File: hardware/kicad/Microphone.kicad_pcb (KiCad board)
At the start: 2 copper layers, 60.1 x 40 mm, 24 parts, among them J1 POWER IN - 5V, J2 AUDIO OUT, U1 OPA1652D

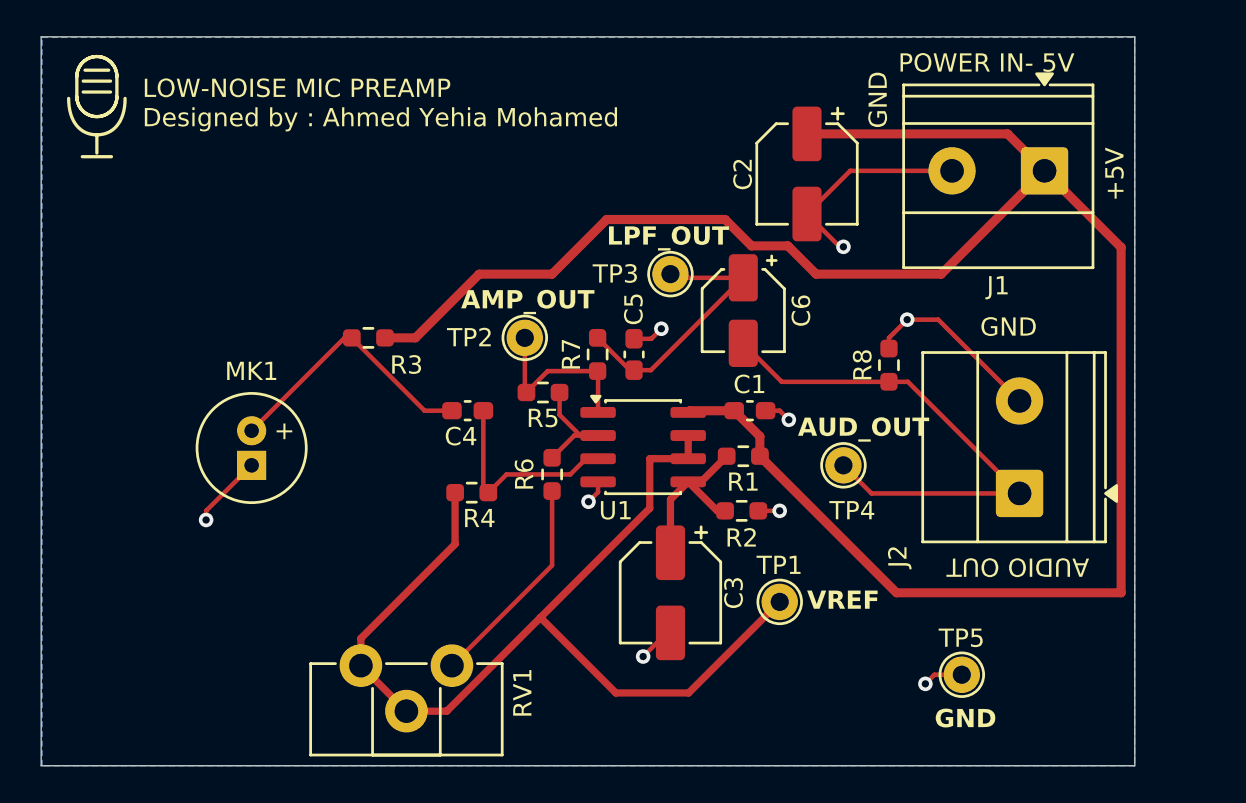
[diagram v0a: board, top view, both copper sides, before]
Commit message: Update microphone preamplifier PCB layout and schematic
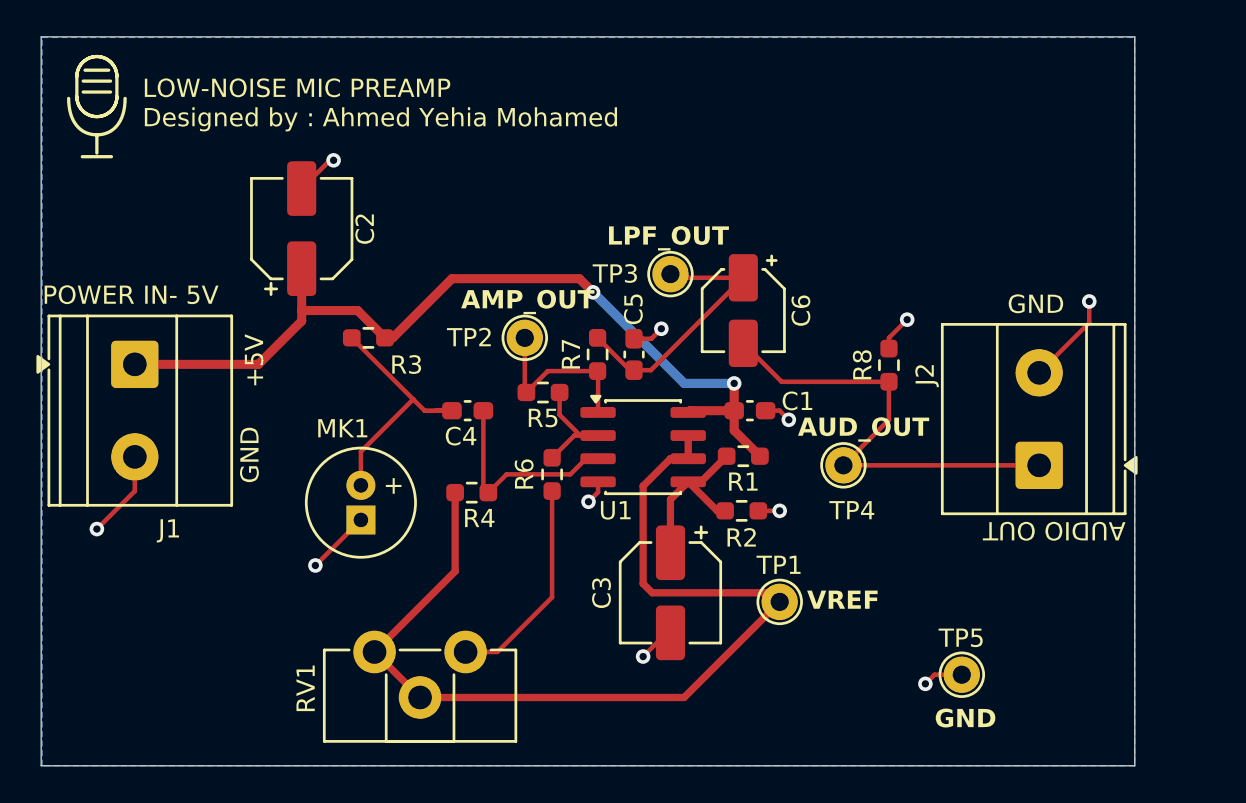
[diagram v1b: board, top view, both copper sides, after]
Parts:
- moved J1 51.1 mm to (105.1, 73.5), turned to -90 degrees
- moved C2 27.9 mm to (114.2, 66.0), turned to 90 degrees
- moved MK1 6.71 mm to (117.5, 81.0)
- moved J2 1.88 mm to (154.8, 79.0)
- moved RV1 1.06 mm to (123.2, 89.2)
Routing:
- net +5V: track 109.9 -> 48.3 mm, vias 0 -> 2
- net GND: track 35.7 -> 27.8 mm, vias 9 -> 11
- net /AUDIO_OUT: track 28.9 -> 25.2 mm
- net /VREF: track 56.2 -> 53.7 mm
- net /MIC_OUT: track 14.8 -> 14.0 mm

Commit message: Sync KiCad sources to manufactured AD8656 revision
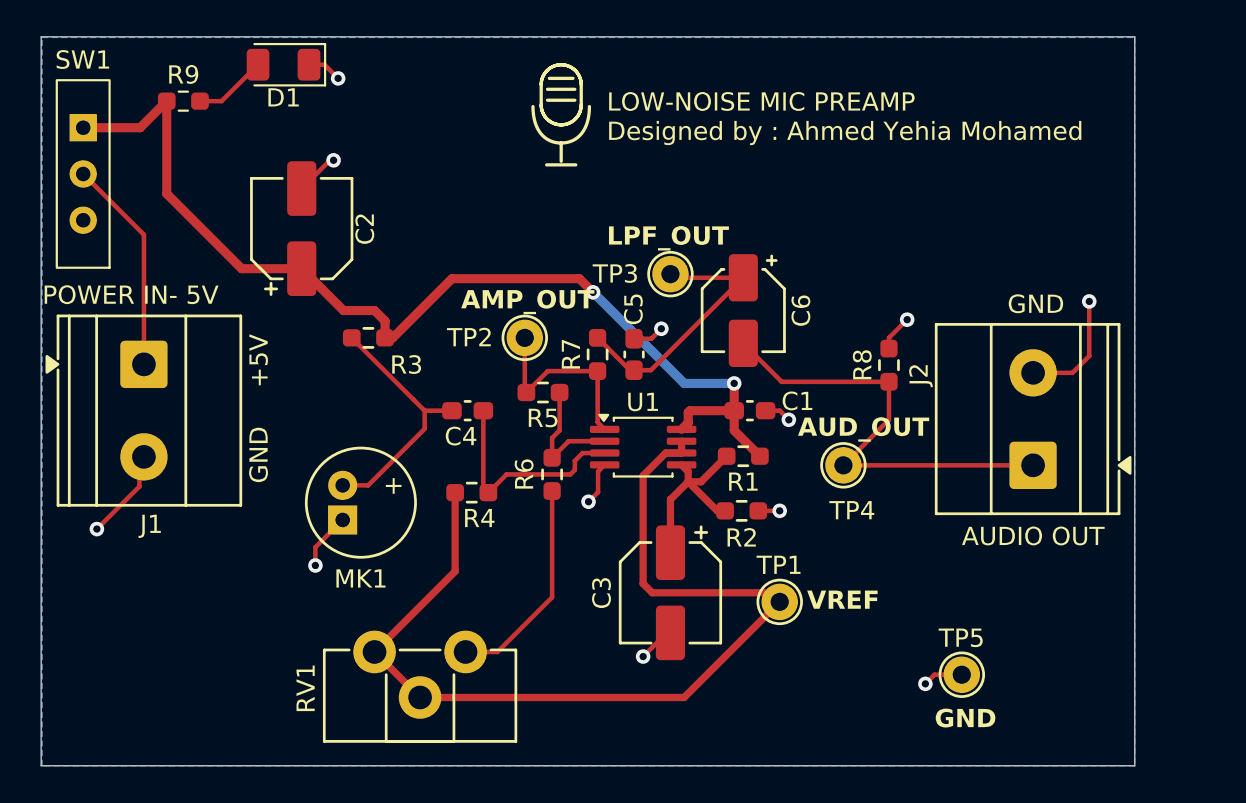
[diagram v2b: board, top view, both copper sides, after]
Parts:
- added D1: LED, LED_SMD:LED_1206_3216Metric, F.Cu at (113.2, 57.0)
- added R9: 2.2k, Resistor_SMD:R_0603_1608Metric_Pad0.98x0.95mm_HandSolder, F.Cu at (107.8, 59.0)
- added SW1: SW_SPDT, AudioPreamp:SW_ESP1010_SPDT_Vertical, F.Cu at (102.2, 63.0)
- U1: value OPA1652D -> AD8656; footprint Package_SO:SOIC-8_3.9x4.9mm_P1.27mm -> Package_SO:MSOP-8_3x3mm_P0.65mm
- moved J1 0.50 mm to (105.6, 73.5)
- moved J2 0.34 mm to (154.4, 79.0)
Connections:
- J1 pad 1: +5V -> Net-(J1-Pin_1)
- MK1 pad 1: GND -> /MIC_OUT
- MK1 pad 2: /MIC_OUT -> GND
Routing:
- net Net-(J1-Pin_1): track 0.00 -> 11.8 mm
- net +5V: track 48.3 -> 57.2 mm
- net GND: track 27.8 -> 31.8 mm, vias 11 -> 12
- net Net-(D1-A): track 0.00 -> 4.02 mm
- net /AMP_OUT: track 9.72 -> 10.8 mm
- net /VREF_RAW: track 9.68 -> 10.8 mm
- net /VREF: track 53.7 -> 53.2 mm
